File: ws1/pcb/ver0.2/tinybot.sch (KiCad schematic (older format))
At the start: 18 parts, among them IC1 ATTINY84-P, P1 PWR, P2 PIN Breakout, P3 ICSP, P4 M1, P5 M2, U1 LD1117S33TR, U2 L293D

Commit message: updated
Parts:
- C1: footprint Capacitors_ThroughHole:C_Disc_D3_P2.5 -> Capacitors_SMD:C_0603
- C2: footprint Capacitors_ThroughHole:C_Radial_D5_L11_P2.5 -> Capacitors_SMD:C_0603
- D1: footprint LEDs:LED-5MM -> LEDs:LED_1206
- IC1: footprint Housings_DIP:DIP-14_W7.62mm -> Housings_SOIC:SOIC-14_3.9x8.7mm_Pitch1.27mm
- JP2: footprint Pin_Headers:Pin_Header_Straight_1x02 -> tinybot:2P-1.27
- P4, P5: footprint Pin_Headers:Pin_Header_Straight_1x02 -> Terminal_Blocks:TerminalBlock_Pheonix_MPT-2.54mm_2pol
- R1, R2, R3: footprint Resistors_ThroughHole:Resistor_Horizontal_RM10mm -> Resistors_SMD:R_0603
- U1: footprint Power_Integrations:TO-220 -> tinybot:SOT-223
- U2: footprint Housings_DIP:DIP-16_W7.62mm -> Housings_SOIC:SOIC-16_7.5x10.3mm_Pitch1.27mm
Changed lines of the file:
@@
 Title "tinyBot"
 Date ""
-Rev "0.2"
+Rev "0.3"
 Comp "electronut Labs"
 Comment1 ""
@@
 F 0 "IC1" H 4850 5350 50  0000 C CNN
 F 1 "ATTINY84-P" H 6400 3850 50  0000 C CNN
-F 2 "Housings_DIP:DIP-14_W7.62mm" H 5700 4400 50  0000 C CIN
+F 2 "Housings_SOIC:SOIC-14_3.9x8.7mm_Pitch1.27mm" H 5700 4400 50  0000 C CIN
 F 3 "" H 5700 4600 50  0000 C CNN
 	1    5700 4600
@@
 F 0 "D1" H 3600 4400 50  0000 C CNN
 F 1 "RED LED" H 3600 4200 50  0000 C CNN
-F 2 "LEDs:LED-5MM" H 3600 4300 50  0001 C CNN
+F 2 "LEDs:LED_1206" H 3600 4300 50  0001 C CNN
 F 3 "" H 3600 4300 50  0000 C CNN
 	1    3600 4300
@@
 F 0 "U2" H 5750 1850 60  0000 C CNN
 F 1 "L293D" H 5750 2850 60  0000 C CNN
-F 2 "Housings_DIP:DIP-16_W7.62mm" H 5850 2350 60  0001 C CNN
+F 2 "Housings_SOIC:SOIC-16_7.5x10.3mm_Pitch1.27mm" H 5850 2350 60  0001 C CNN
 F 3 "" H 5850 2350 60  0000 C CNN
 	1    5750 2350
@@
 F 0 "R2" V 8280 3700 50  0000 C CNN
 F 1 "330" V 8200 3700 50  0000 C CNN
-F 2 "Resistors_ThroughHole:Resistor_Horizontal_RM10mm" V 8130 3700 50  0001 C CNN
+F 2 "Resistors_SMD:R_0603" V 8130 3700 50  0001 C CNN
 F 3 "" H 8200 3700 50  0000 C CNN
 	1    8200 3700
@@
 F 0 "R3" V 8280 4000 50  0000 C CNN
 F 1 "330" V 8200 4000 50  0000 C CNN
-F 2 "Resistors_ThroughHole:Resistor_Horizontal_RM10mm" V 8130 4000 50  0001 C CNN
+F 2 "Resistors_SMD:R_0603" V 8130 4000 50  0001 C CNN
 F 3 "" H 8200 4000 50  0000 C CNN
 	1    8200 4000
@@
 F 0 "U1" H 2700 4300 50  0000 C CNN
 F 1 "LD1117S33TR" H 2700 4250 50  0000 C CNN
-F 2 "Power_Integrations:TO-220" H 2700 4150 50  0000 C CNN
+F 2 "tinybot:SOT-223" H 2700 4150 50  0000 C CNN
 F 3 "" H 2700 4050 50  0000 C CNN
 	1    2700 4050
@@
 F 0 "R1" V 3680 4950 50  0000 C CNN
 F 1 "330" V 3600 4950 50  0000 C CNN
-F 2 "Resistors_ThroughHole:Resistor_Horizontal_RM10mm" V 3530 4950 50  0001 C CNN
+F 2 "Resistors_SMD:R_0603" V 3530 4950 50  0001 C CNN
 F 3 "" H 3600 4950 50  0000 C CNN
 	1    3600 4950
@@
 F 0 "P4" H 3900 2400 50  0000 C CNN
 F 1 "M1" V 4000 2250 50  0000 C CNN
-F 2 "Pin_Headers:Pin_Header_Straight_1x02" H 3900 2250 50  0001 C CNN
+F 2 "Terminal_Blocks:TerminalBlock_Pheonix_MPT-2.54mm_2pol" H 3900 2250 50  0001 C CNN
 F 3 "" H 3900 2250 50  0000 C CNN
 	1    3900 2250
@@
 F 0 "P5" H 7700 2400 50  0000 C CNN
 F 1 "M2" V 7800 2250 50  0000 C CNN
-F 2 "Pin_Headers:Pin_Header_Straight_1x02" H 7700 2250 50  0001 C CNN
+F 2 "Terminal_Blocks:TerminalBlock_Pheonix_MPT-2.54mm_2pol" H 7700 2250 50  0001 C CNN
 F 3 "" H 7700 2250 50  0000 C CNN
 	1    7700 2250
@@
 F 0 "JP2" H 4300 1850 50  0000 C CNN
 F 1 "JUMPER" H 4300 1620 50  0000 C CNN
-F 2 "Pin_Headers:Pin_Header_Straight_1x02" H 4300 1700 50  0001 C CNN
+F 2 "tinybot:2P-1.27" H 4300 1700 50  0001 C CNN
 F 3 "" H 4300 1700 50  0000 C CNN
 	1    4300 1700
@@
 F 0 "C1" H 2225 4450 50  0000 L CNN
 F 1 "0.1uF" H 2225 4250 50  0000 L CNN
-F 2 "Capacitors_ThroughHole:C_Disc_D3_P2.5" H 2238 4200 50  0001 C CNN
+F 2 "Capacitors_SMD:C_0603" H 2238 4200 50  0001 C CNN
 F 3 "" H 2200 4350 50  0000 C CNN
 	1    2200 4350
@@
 F 0 "C2" H 3225 4450 50  0000 L CNN
 F 1 "10uF" H 3225 4250 50  0000 L CNN
-F 2 "Capacitors_ThroughHole:C_Radial_D5_L11_P2.5" H 3238 4200 50  0001 C CNN
+F 2 "Capacitors_SMD:C_0603" H 3238 4200 50  0001 C CNN
 F 3 "" H 3200 4350 50  0000 C CNN
 	1    3200 4350

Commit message: logo added
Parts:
- P1: footprint Pin_Headers:Pin_Header_Straight_1x02 -> Terminal_Blocks:TerminalBlock_Pheonix_MPT-2.54mm_2pol
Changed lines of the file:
@@
 F 0 "P1" H 1500 4200 50  0000 C CNN
 F 1 "PWR" V 1600 4050 50  0000 C CNN
-F 2 "Pin_Headers:Pin_Header_Straight_1x02" H 1500 4050 50  0001 C CNN
+F 2 "Terminal_Blocks:TerminalBlock_Pheonix_MPT-2.54mm_2pol" H 1500 4050 50  0001 C CNN
 F 3 "" H 1500 4050 50  0000 C CNN
 	1    1500 4050

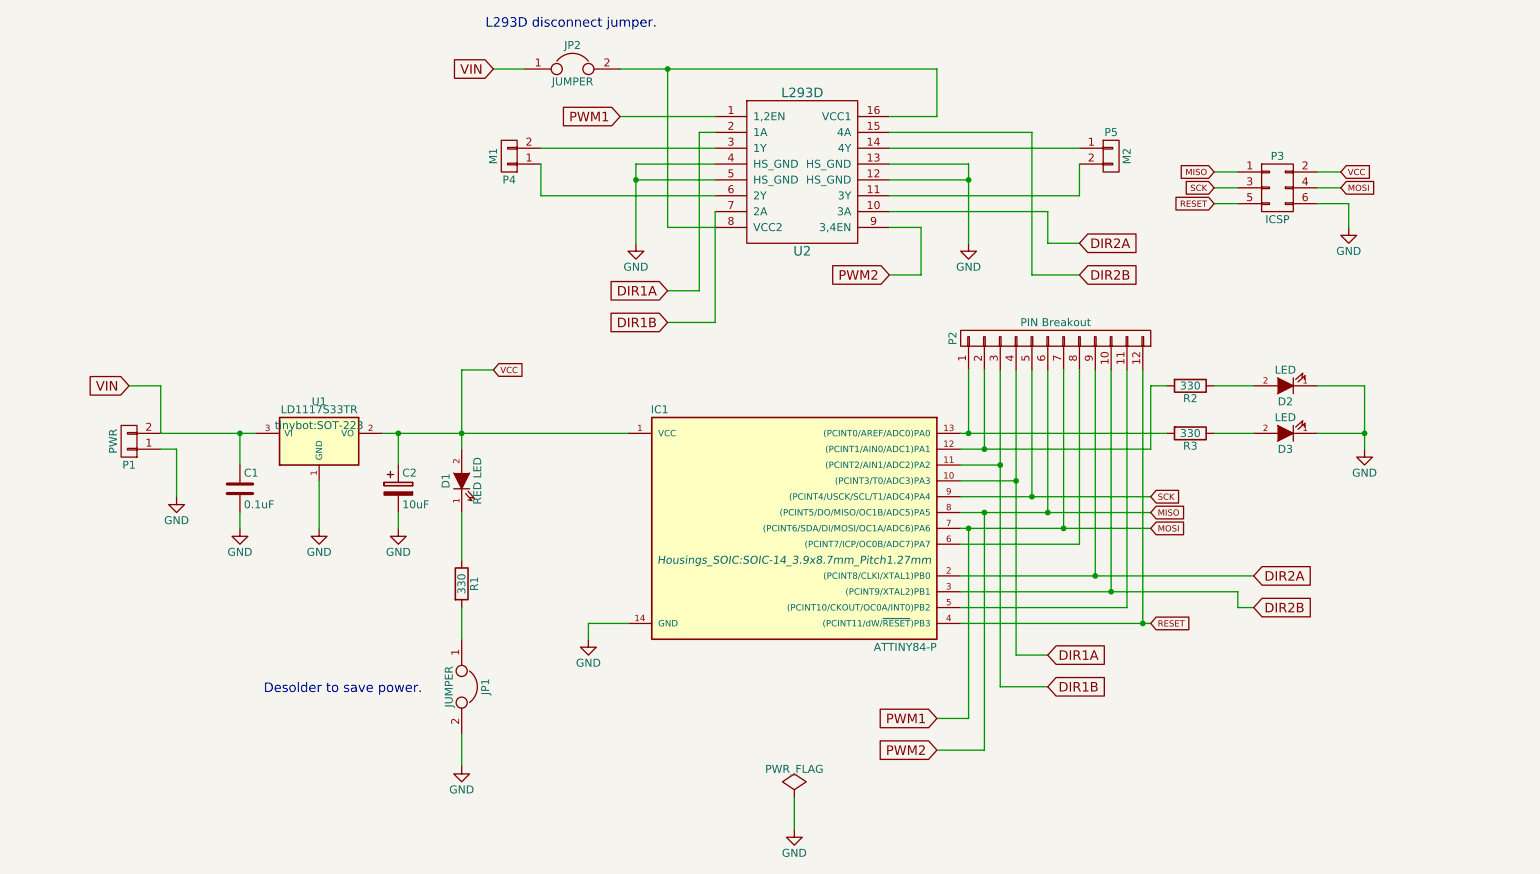
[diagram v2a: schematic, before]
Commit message: switched to rgb led
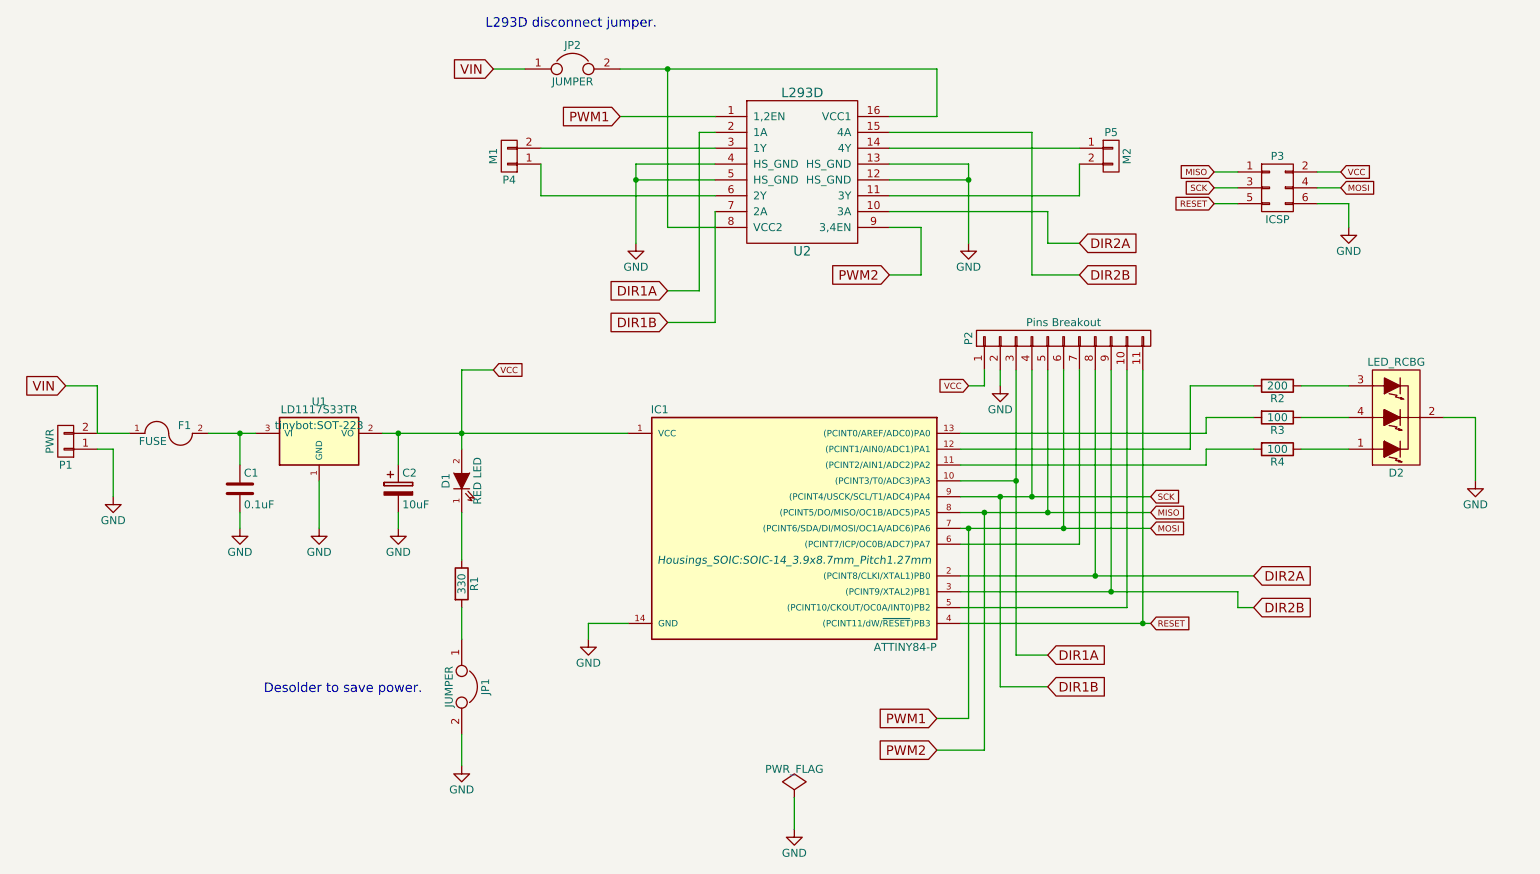
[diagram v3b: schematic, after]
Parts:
- removed D2, D3: LED, LEDs:LED-5MM, symbol LED
- removed P2: PIN Breakout, Pin_Headers:Pin_Header_Straight_1x12, symbol CONN_01X12
- added D2: LED_RCBG, LEDs:LED-RGB-5MM_Common_Cathode, symbol LED_RCBG
- added F1: FUSE, Fuse_Holders_and_Fuses:Fuse_SMD1206_Reflow, symbol FUSE
- added P2: Pins Breakout, Pin_Headers:Pin_Header_Straight_1x11, symbol CONN_01X11
- added R4: 100, Resistors_SMD:R_0603, symbol R
- R2: value 330 -> 200
- R3: value 330 -> 100
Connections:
- net SCK is gone; now on net DIR1B: IC1.9 ((PCINT4/USCK/SCL/T1/ADC4)PA4), P3.3 (P3)
- net DIR1A: now also P2.3 (P3)
- net DIR1B: now also P2.4 (P4); no longer IC1.11 ((PCINT2/AIN1/ADC2)PA2)
- net DIR2A: now also P2.8 (P8)
- net DIR2B: now also P2.9 (P9)
- net GND: now also D2.2 (COMMON_CATHODE), P2.2 (P2)
- net MISO: now also P2.5 (P5)
- net MOSI: now also P2.6 (P6)
- net RESET: now also P2.11 (P11)
- net VCC: now also P2.1 (P1)
- net VIN: now also F1.1; no longer C1.1, U1.3 (VI)
- net at IC1.5 ((PCINT10/CKOUT/OC0A/INT0)PB2): now also P2.10 (P10)
- net at IC1.6 ((PCINT7/ICP/OC0B/ADC7)PA7): now also P2.7 (P7)
- net at R3.1: now also D2.4 (GREEN_ANODE)
- net at R2.1: now also D2.3 (BLUE_ANODE)
- new net: IC1.11 ((PCINT2/AIN1/ADC2)PA2), R4.2
- new net: C1.1, F1.2, U1.3 (VI)
- new net: D2.1 (RED_ANODE), R4.1
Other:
- moved on the sheet: P1, R2, R3

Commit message: refining PCB
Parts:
- removed P2: Pins Breakout, Pin_Headers:Pin_Header_Straight_1x11, symbol CONN_01X11
- added JP3: JUMPER, Capacitors_SMD:C_0402, symbol JUMPER
- added P2: Pin Breakout, tinybot:Pin_Header_Straight_1x14, symbol CONN_01X14
- JP2: footprint tinybot:2P-1.27 -> Capacitors_SMD:C_0402
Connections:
- net DIR1A: now also P2.6 (P6)
- net DIR1B: now also P2.7 (P7)
- net DIR2A: now also P2.11 (P11)
- net DIR2B: now also P2.12 (P12)
- net GND: now also JP3.2, P2.2 (P2); no longer D2.2 (COMMON_CATHODE)
- net MISO: now also P2.8 (P8)
- net MOSI: now also P2.9 (P9)
- net RESET: now also P2.14 (P14)
- net VCC: now also P2.1 (P1)
- net at IC1.11 ((PCINT2/AIN1/ADC2)PA2), R4.2: now also P2.5 (P5)
- net at IC1.12 ((PCINT1/AIN0/ADC1)PA1), R2.2: now also P2.4 (P4)
- net at IC1.13 ((PCINT0/AREF/ADC0)PA0), R3.2: now also P2.3 (P3)
- net at IC1.5 ((PCINT10/CKOUT/OC0A/INT0)PB2): now also P2.13 (P13)
- net at IC1.6 ((PCINT7/ICP/OC0B/ADC7)PA7): now also P2.10 (P10)
- new net: D2.2 (COMMON_CATHODE), JP3.1
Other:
- note added: "Power LED disconnect jumper."
- note added: "RGB LED disconnet jumper."
- note removed: "Desolder to save power."
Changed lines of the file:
@@
 Text GLabel 8350 2550 0    39   Input ~ 0
 RESET
-Text Notes 2350 5650 0    60   ~ 0
-Desolder to save power.
+Text Notes 3700 5850 0    60   ~ 0
+Power LED disconnect jumper.
 $Comp
 L CONN_01X02 P4
@@
 F 0 "JP2" H 4300 1850 50  0000 C CNN
 F 1 "JUMPER" H 4300 1620 50  0000 C CNN
-F 2 "tinybot:2P-1.27" H 4300 1700 50  0001 C CNN
+F 2 "Capacitors_SMD:C_0402" H 4300 1700 50  0001 C CNN
 F 3 "" H 4300 1700 50  0000 C CNN
 	1    4300 1700
@@
 L GND #PWR012
 U 1 1 56DD94E5
-P 10000 4300
-F 0 "#PWR012" H 10000 4050 50  0001 C CNN
-F 1 "GND" H 10000 4150 50  0000 C CNN
-F 2 "" H 10000 4300 50  0000 C CNN
-F 3 "" H 10000 4300 50  0000 C CNN
-	1    10000 4300
-	1    0    0    -1
-$EndComp
-Text GLabel 6800 3700 0    39   Input ~ 0
+P 10000 5100
+F 0 "#PWR012" H 10000 4850 50  0001 C CNN
+F 1 "GND" H 10000 4950 50  0000 C CNN
+F 2 "" H 10000 5100 50  0000 C CNN
+F 3 "" H 10000 5100 50  0000 C CNN
+	1    10000 5100
+	1    0    0    -1
+$EndComp
+Text GLabel 6500 3700 0    39   Input ~ 0
 VCC
 $Comp
 L GND #PWR013
 U 1 1 56DDA4AD
-P 7000 3700
-F 0 "#PWR013" H 7000 3450 50  0001 C CNN
-F 1 "GND" H 7000 3550 50  0000 C CNN
-F 2 "" H 7000 3700 50  0000 C CNN
-F 3 "" H 7000 3700 50  0000 C CNN
-	1    7000 3700
-	1    0    0    -1
-$EndComp
-$Comp
-L CONN_01X11 P2
-U 1 1 56DE540A
-P 7400 3400
-F 0 "P2" H 7400 4000 50  0000 C CNN
-F 1 "Pins Breakout" V 7500 3400 50  0000 C CNN
-F 2 "Pin_Headers:Pin_Header_Straight_1x11" H 7400 3400 50  0001 C CNN
-F 3 "" H 7400 3400 50  0000 C CNN
-	1    7400 3400
-	0    -1   -1   0
-$EndComp
+P 6700 3700
+F 0 "#PWR013" H 6700 3450 50  0001 C CNN
+F 1 "GND" H 6700 3550 50  0000 C CNN
+F 2 "" H 6700 3700 50  0000 C CNN
+F 3 "" H 6700 3700 50  0000 C CNN
+	1    6700 3700
+	1    0    0    -1
+$EndComp
+$Comp
+L JUMPER JP3
+U 1 1 56DE6039
+P 10000 4600
+F 0 "JP3" H 10000 4750 50  0000 C CNN
+F 1 "JUMPER" H 10000 4520 50  0000 C CNN
+F 2 "Capacitors_SMD:C_0402" H 10000 4600 50  0001 C CNN
+F 3 "" H 10000 4600 50  0000 C CNN
+	1    10000 4600
+	0    1    1    0
+$EndComp
+Text Notes 10300 3950 3    60   ~ 0
+RGB LED disconnet jumper.
 Wire Wire Line
 	3800 1700 4000 1700
@@
 	6750 4100 8200 4100
 Wire Wire Line
-	7000 3600 7000 3700
-Wire Wire Line
-	6900 3600 6900 3700
-Wire Wire Line
-	6900 3700 6800 3700
+	6700 3600 6700 3700
+Wire Wire Line
+	6600 3600 6600 3700
+Wire Wire Line
+	6600 3700 6500 3700
 Wire Wire Line
 	7000 5600 7000 4400
 Connection ~ 7000 4400
+Wire Wire Line
+	10000 4900 10000 5100
+Wire Wire Line
+	6800 3600 6800 4000
+Connection ~ 6800 4000
+Wire Wire Line
+	6900 3600 6900 4100
+Connection ~ 6900 4100
+Wire Wire Line
+	7000 3600 7000 4200
+Connection ~ 7000 4200
+$Comp
+L CONN_01X14 P2
+U 1 1 56DE6C96
+P 7250 3400
+F 0 "P2" H 7250 4150 50  0000 C CNN
+F 1 "Pin Breakout" V 7350 3400 50  0000 C CNN
+F 2 "tinybot:Pin_Header_Straight_1x14" H 7250 3400 50  0001 C CNN
+F 3 "" H 7250 3400 50  0000 C CNN
+	1    7250 3400
+	0    -1   -1   0
+$EndComp
+Text GLabel 5000 6500 2    60   Input ~ 0
+VIN
+$Comp
+L PWR_FLAG #FLG?
+U 1 1 56DE7431
+P 4900 6300
+F 0 "#FLG?" H 4900 6395 50  0001 C CNN
+F 1 "PWR_FLAG" H 4900 6480 50  0000 C CNN
+F 2 "" H 4900 6300 50  0000 C CNN
+F 3 "" H 4900 6300 50  0000 C CNN
+	1    4900 6300
+	1    0    0    -1
+$EndComp
+Wire Wire Line
+	4900 6300 4900 6500
+Wire Wire Line
+	4900 6500 5000 6500
 $EndSCHEMATC

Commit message: switching to DRV8835
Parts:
- U2: footprint Housings_SOIC:SOIC-16_7.5x10.3mm_Pitch1.27mm -> Housings_SOIC:SOIC-20_7.5x12.8mm_Pitch1.27mm
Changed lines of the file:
@@
 F 0 "U2" H 5750 1850 60  0000 C CNN
 F 1 "L293D" H 5750 2850 60  0000 C CNN
-F 2 "Housings_SOIC:SOIC-16_7.5x10.3mm_Pitch1.27mm" H 5850 2350 60  0001 C CNN
+F 2 "Housings_SOIC:SOIC-20_7.5x12.8mm_Pitch1.27mm" H 5850 2350 60  0001 C CNN
 F 3 "" H 5850 2350 60  0000 C CNN
 	1    5750 2350
@@
 VIN
 $Comp
-L PWR_FLAG #FLG?
+L PWR_FLAG #FLG014
 U 1 1 56DE7431
 P 4900 6300
-F 0 "#FLG?" H 4900 6395 50  0001 C CNN
+F 0 "#FLG014" H 4900 6395 50  0001 C CNN
 F 1 "PWR_FLAG" H 4900 6480 50  0000 C CNN
 F 2 "" H 4900 6300 50  0000 C CNN
